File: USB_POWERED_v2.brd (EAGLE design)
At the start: 39.4 x 17.8 mm, 16 parts, among them J1 USB

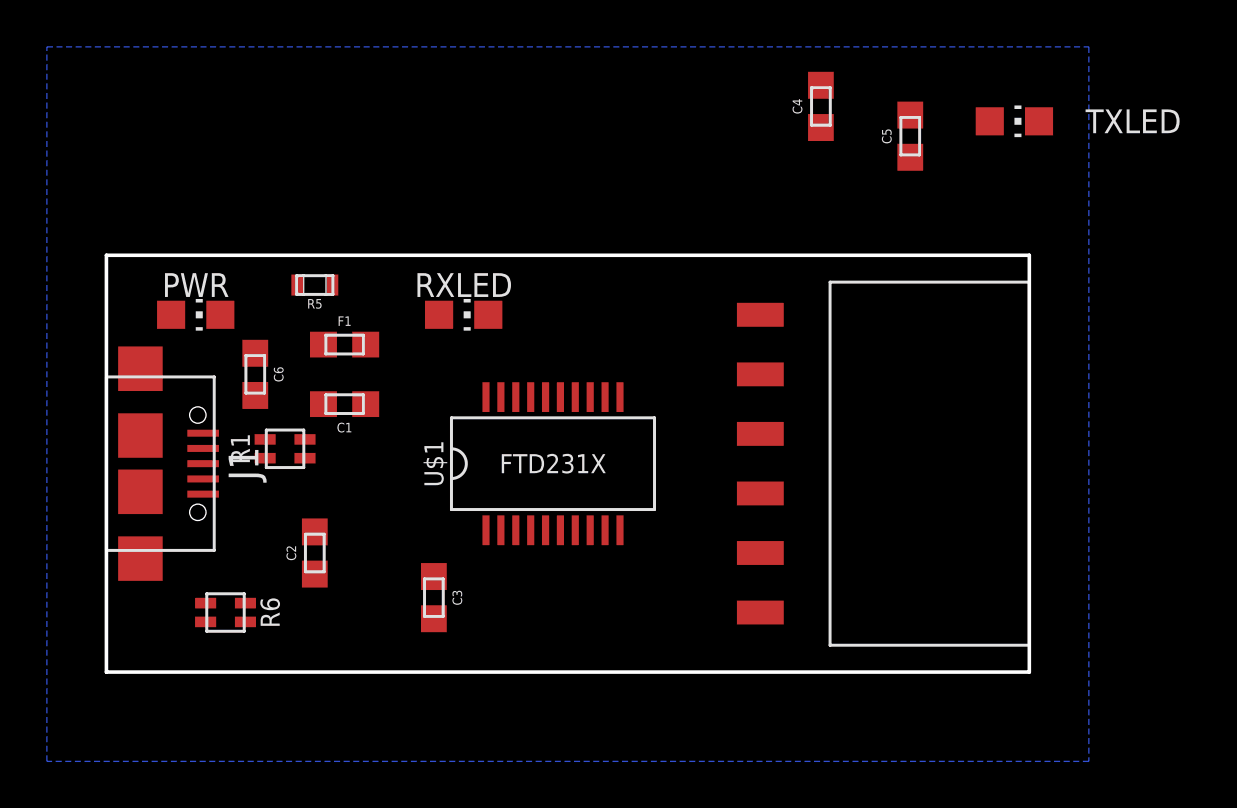
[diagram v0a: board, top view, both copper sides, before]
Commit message: update routing. Will probably change again before file is sent...
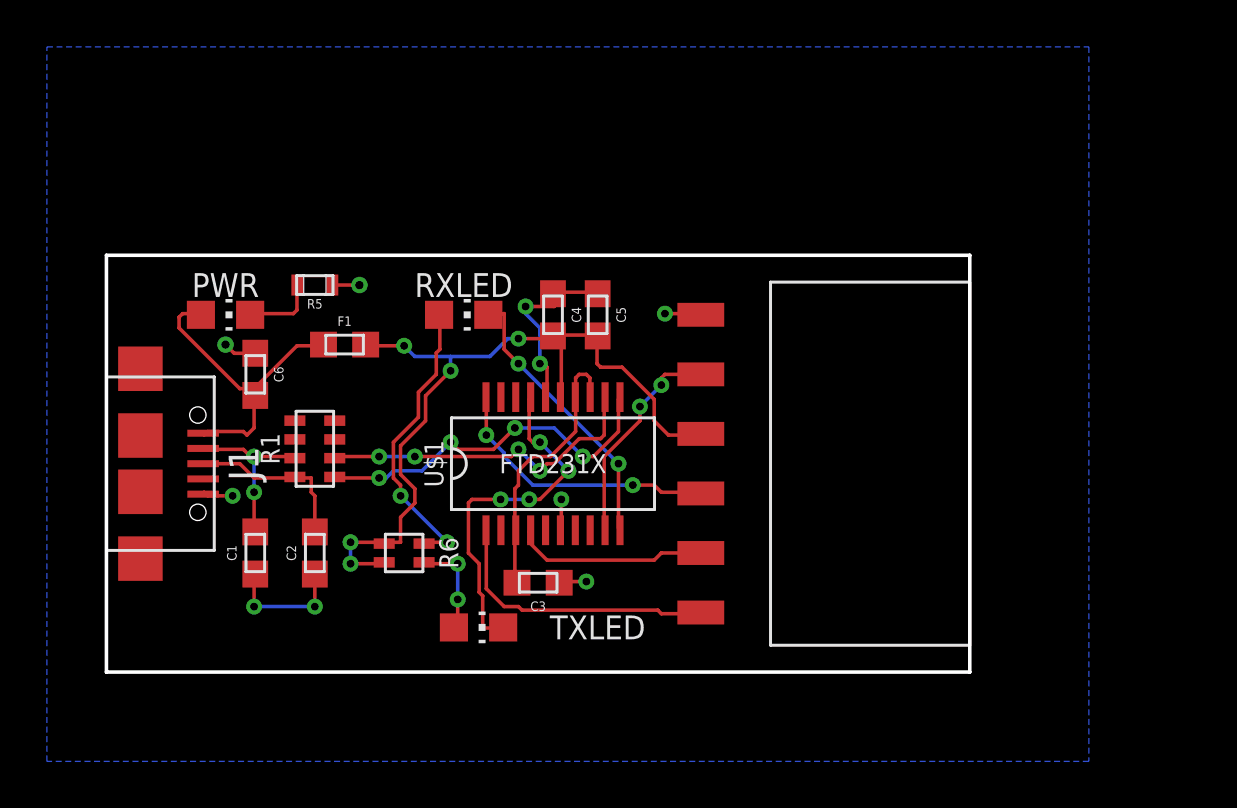
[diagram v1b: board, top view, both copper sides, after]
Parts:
- R1: device ERIC:RESISTOR_ARRAY_CTS_742C043 -> ERIC:RESISTOR_ARRAY_CTS_742_4
- moved TXLED 31.4 mm to (33.7, 8.26)
- moved C5 15.4 mm to (38.7, 21.6), turned to 270 degrees
- moved C4 14.5 mm to (36.8, 21.6), turned to 270 degrees
- moved R6 8.03 mm to (30.5, 11.4)
- moved C1 7.41 mm to (24.1, 11.4), turned to 90 degrees
- moved C3 4.49 mm to (36.2, 10.2), turned to 180 degrees
- moved U$2 2.54 mm to (54.6, 15.2)
- moved R1 1.27 mm to (26.7, 15.9)
- moved PWR 1.27 mm to (22.9, 21.6)
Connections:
- net N$1: now also R1.P$3; no longer R1.P$5
- net N$2: now also R1.P$1; no longer R1.P$3
- net N$4: now also R1.P$4; no longer R1.P$6
- net N$5: now also R1.P$2; no longer R1.P$4
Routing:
- net VCC: track 0.00 -> 34.8 mm, vias 0 -> 5
- net GND: track 0.00 -> 21.5 mm, vias 0 -> 10
- net N$2: track 0.00 -> 15.7 mm, vias 0 -> 4
- net N$9: track 0.00 -> 15.3 mm, vias 0 -> 4
- net USB_POWER: track 0.00 -> 14.5 mm
- net N$1: track 0.00 -> 14.3 mm, vias 0 -> 4
- net N$7: track 0.00 -> 12.5 mm, vias 0 -> 2
- net DTR: track 0.00 -> 12.1 mm
- net N$8: track 0.00 -> 12.0 mm, vias 0 -> 2
- net 3V3OUT: track 0.00 -> 11.9 mm
- net TXO: track 0.00 -> 11.9 mm, vias 0 -> 2
- net CTS: track 0.00 -> 9.26 mm, vias 0 -> 2
- net RXI: track 0.00 -> 8.30 mm
- net N$4: track 0.00 -> 7.34 mm, vias 0 -> 2
- net N$5: track 0.00 -> 7.25 mm
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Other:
- board size 39.4 x 17.8 mm -> 36.8 x 17.8 mm
- board text added: "14Sep2017"
- board text added: "v2"
- board text removed: "26July2017"
- board text removed: "v1"
